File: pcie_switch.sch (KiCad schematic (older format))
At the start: 61 parts

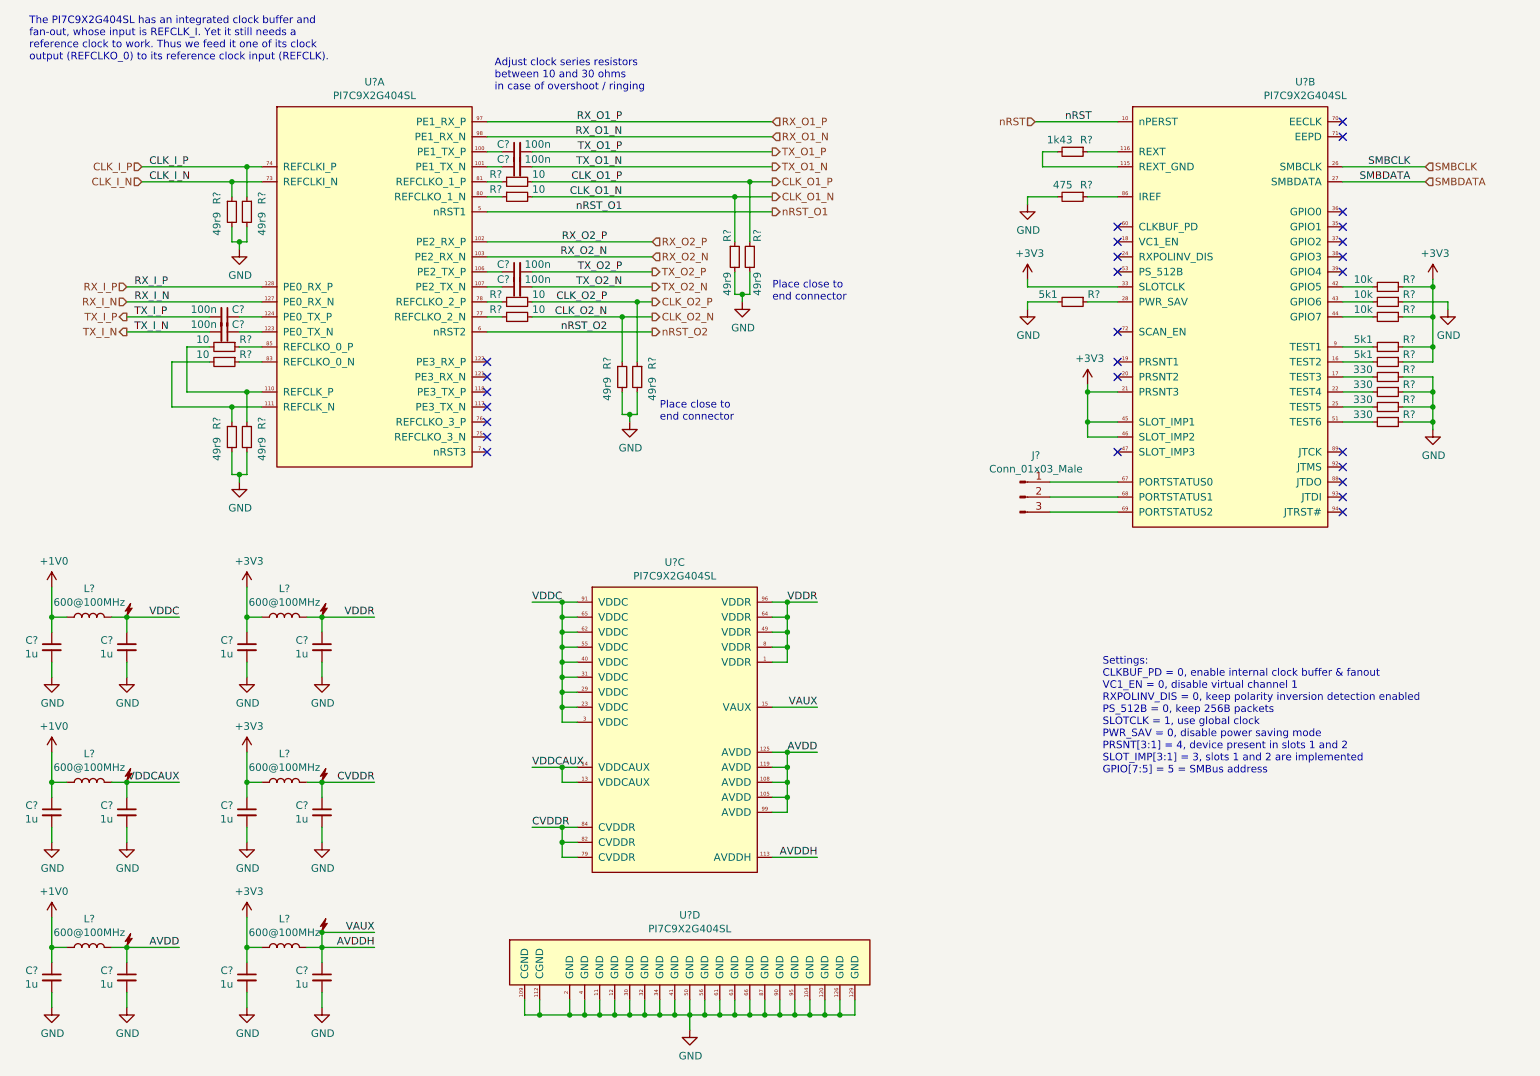
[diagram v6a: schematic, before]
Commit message: sch: Annotate & associate symbols with footprints
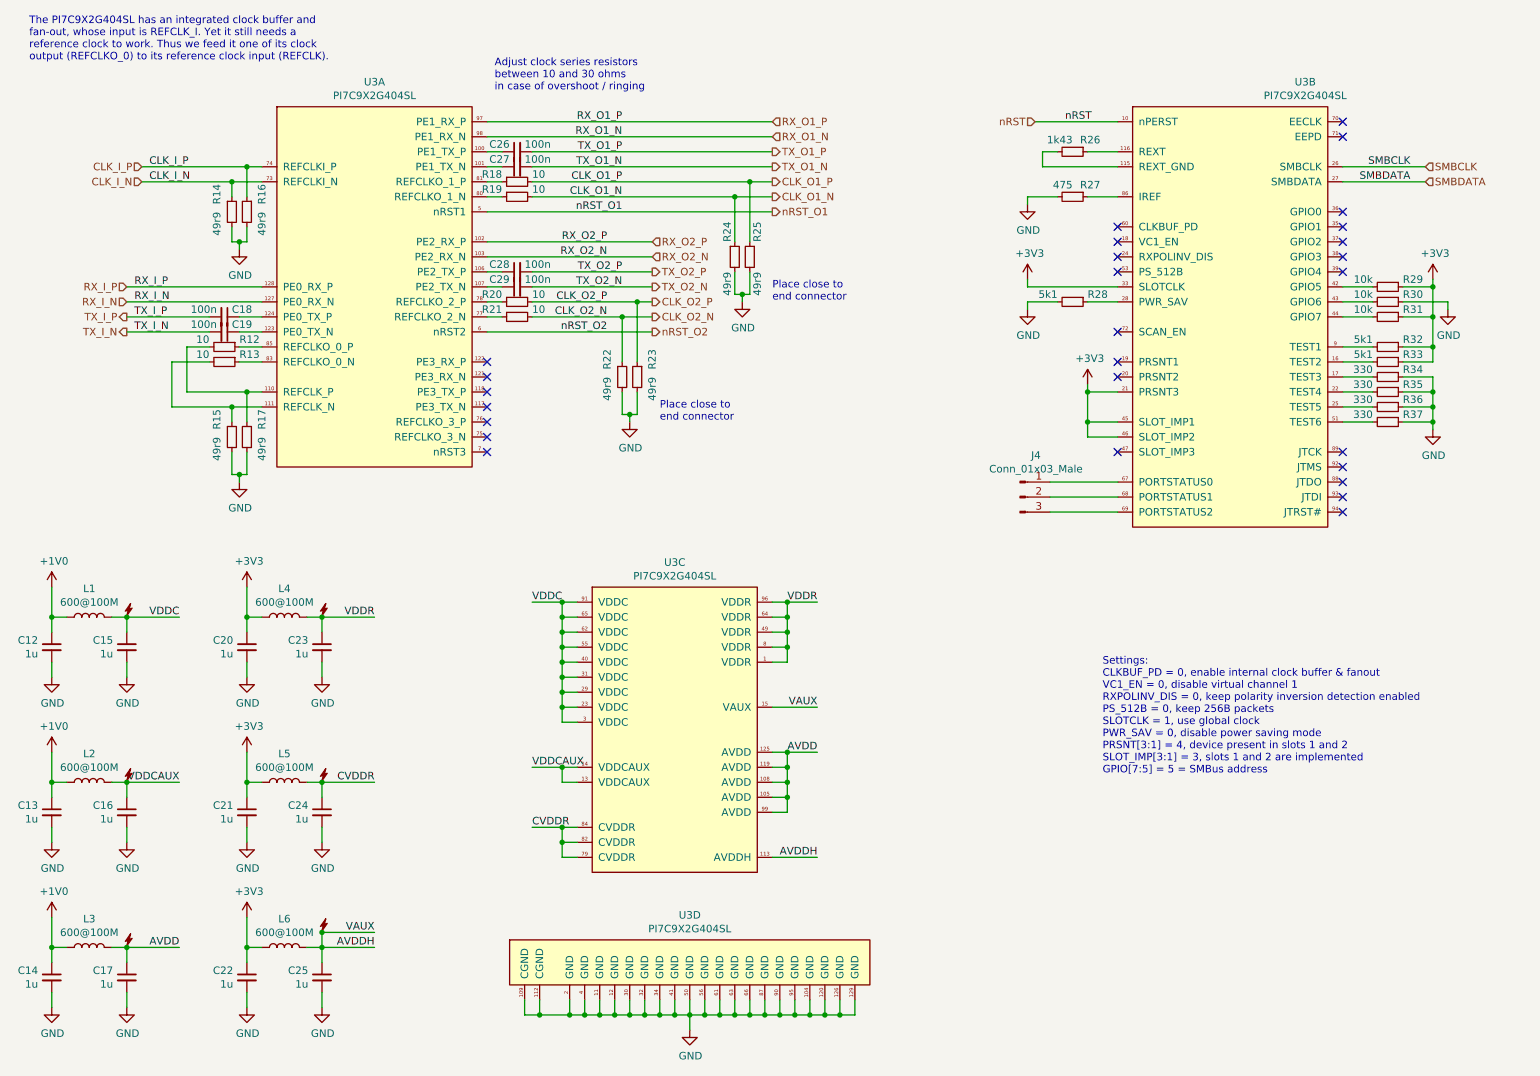
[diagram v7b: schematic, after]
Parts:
- removed DS? (x6): DummySupply, symbol pimouss-motherboard:DummySupply
- C12, C13, C14, C15, C16, C17, C20, C21, C22, C23, C24, C25: renamed from C?; footprint (none) -> Capacitor_SMD:C_0603_1608Metric
- C18, C19, C26, C27, C28, C29: renamed from C?; footprint (none) -> Capacitor_SMD:C_0402_1005Metric
- J4: renamed from J?; footprint (none) -> Connector_PinHeader_2.54mm:PinHeader_1x03_P2.54mm_Vertical
- L1, L2, L3, L4, L5, L6: renamed from L?; value 600@100MHz -> 600@100M; footprint (none) -> Inductor_SMD:L_0603_1608Metric
- R12, R13, R14, R15, R16, R17, R18, R19, R20, R21, R22, R23, R24, R25: renamed from R?; footprint (none) -> Resistor_SMD:R_0402_1005Metric
- R26, R27, R28, R29, R30, R31, R32, R33, R34, R35, R36, R37: renamed from R?; footprint (none) -> Resistor_SMD:R_0603_1608Metric
- gave numbers to parts that had none: 1

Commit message: lib, sch: Fix connectors refdes letter
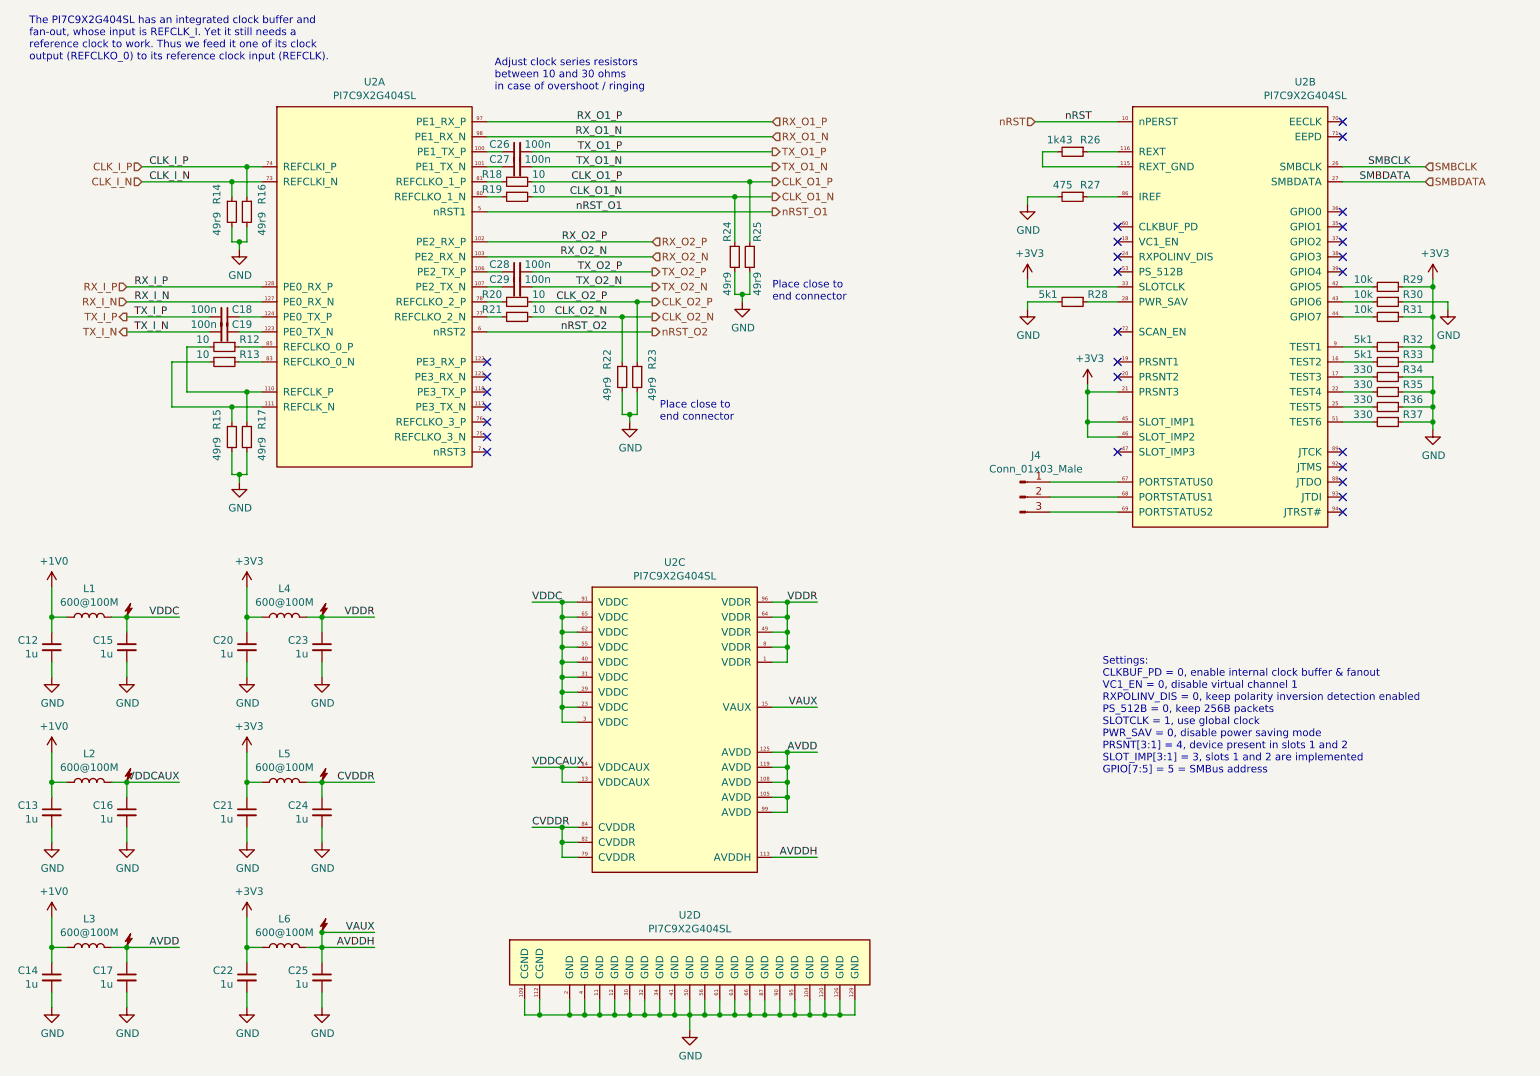
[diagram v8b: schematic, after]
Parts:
- renumbered U3 to U2
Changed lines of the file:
@@
 $EndDescr
 $Comp
-L pimouss-motherboard:PI7C9X2G404SL U3
+L pimouss-motherboard:PI7C9X2G404SL U2
 U 1 1 5D541909
 P 2400 1400
-F 0 "U3" H 3050 1565 50  0000 C CNN
+F 0 "U2" H 3050 1565 50  0000 C CNN
 F 1 "PI7C9X2G404SL" H 3050 1474 50  0000 C CNN
 F 2 "pimouss-motherboard:LQFP-128_1EP_14x14mm_P0.4mm_EP6x6mm" H 2300 1450 50  0001 C CNN
@@
 $EndComp
 $Comp
-L pimouss-motherboard:PI7C9X2G404SL U3
+L pimouss-motherboard:PI7C9X2G404SL U2
 U 3 1 5D5419FE
 P 4500 4600
-F 0 "U3" H 5050 4765 50  0000 C CNN
+F 0 "U2" H 5050 4765 50  0000 C CNN
 F 1 "PI7C9X2G404SL" H 5050 4674 50  0000 C CNN
 F 2 "pimouss-motherboard:LQFP-128_1EP_14x14mm_P0.4mm_EP6x6mm" H 4400 4650 50  0001 C CNN
@@
 $EndComp
 $Comp
-L pimouss-motherboard:PI7C9X2G404SL U3
+L pimouss-motherboard:PI7C9X2G404SL U2
 U 4 1 5D541A5B
 P 3950 6950
-F 0 "U3" H 5150 7115 50  0000 C CNN
+F 0 "U2" H 5150 7115 50  0000 C CNN
 F 1 "PI7C9X2G404SL" H 5150 7024 50  0000 C CNN
 F 2 "pimouss-motherboard:LQFP-128_1EP_14x14mm_P0.4mm_EP6x6mm" H 3850 7000 50  0001 C CNN
@@
 $EndComp
 $Comp
-L pimouss-motherboard:PI7C9X2G404SL U3
+L pimouss-motherboard:PI7C9X2G404SL U2
 U 2 1 5D5419B0
 P 8100 1400
-F 0 "U3" H 9250 1565 50  0000 C CNN
+F 0 "U2" H 9250 1565 50  0000 C CNN
 F 1 "PI7C9X2G404SL" H 9250 1474 50  0000 C CNN
 F 2 "pimouss-motherboard:LQFP-128_1EP_14x14mm_P0.4mm_EP6x6mm" H 8000 1450 50  0001 C CNN
